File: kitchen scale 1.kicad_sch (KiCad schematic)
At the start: 1 part

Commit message: 2
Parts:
- added BT1: Battery, symbol Device:Battery
- added F1: Fuse, symbol Device:Fuse
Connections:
- new net: BT1.1 (+), F1.2
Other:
- note added: "Power"
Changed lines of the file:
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@@
 	(generator_version "9.0")
 	(paper "A4")
+	(text "Power"
+		(exclude_from_sim no)
+		(at 33.782 155.448 0)
+		(effects
+			(font
+				(size 1.27 1.27)
+			)
+		)
+	)
 	(wire
 		(pts
@@
 		)
 	)
+	(symbol
+		(lib_id "Device:Battery")
+		(at 27.94 173.99 0)
+		(unit 1)
+		(exclude_from_sim no)
+		(in_bom yes)
+		(on_board yes)
+		(dnp no)
+		(fields_autoplaced yes)
+		(property "Reference" "BT1"
+			(at 31.75 172.1484 0)
+			(effects
+				(font
+					(size 1.27 1.27)
+				)
+				(justify left)
+			)
+		)
+		(property "Value" "Battery"
+			(at 31.75 174.6884 0)
+			(effects
+				(font
+					(size 1.27 1.27)
+				)
+				(justify left)
+			)
+		)
+		(property "Footprint" ""
+			(at 27.94 172.466 90)
+			(effects
+				(font
+					(size 1.27 1.27)
+				)
+				(hide yes)
+			)
+		)
+		(property "Datasheet" "~"
+			(at 27.94 172.466 90)
+			(effects
+				(font
+					(size 1.27 1.27)
+				)
+				(hide yes)
+			)
+		)
+		(property "Description" "Multiple-cell battery"
+			(at 27.94 173.99 0)
+			(effects
+				(font
+					(size 1.27 1.27)
+				)
+				(hide yes)
+			)
+		)
+		(property "Sim.Device" "V"
+			(at 27.94 173.99 0)
+			(effects
+				(font
+					(size 1.27 1.27)
+				)
+				(hide yes)
+			)
+		)
+		(property "Sim.Type" "DC"
+			(at 27.94 173.99 0)
+			(effects
+				(font
+					(size 1.27 1.27)
+				)
+				(hide yes)
+			)
+		)
+		(property "Sim.Pins" "1=+ 2=-"
+			(at 27.94 173.99 0)
+			(effects
+				(font
+					(size 1.27 1.27)
+				)
+				(hide yes)
+			)
+		)
+		(pin "1"
+		)
+		(pin "2"
+		)
+		(instances
+			(project ""
+				(path "/e0ae7b4d-acc0-43ca-84de-8c29a2234f1c"
+					(reference "BT1")
+					(unit 1)
+				)
+			)
+		)
+	)
+	(symbol
+		(lib_id "Device:Fuse")
+		(at 27.94 165.1 0)
+		(unit 1)
+		(exclude_from_sim no)
+		(in_bom yes)
+		(on_board yes)
+		(dnp no)
+		(fields_autoplaced yes)
+		(property "Reference" "F1"
+			(at 30.48 163.8299 0)
+			(effects
+				(font
+					(size 1.27 1.27)
+				)
+				(justify left)
+			)
+		)
+		(property "Value" "Fuse"
+			(at 30.48 166.3699 0)
+			(effects
+				(font
+					(size 1.27 1.27)
+				)
+				(justify left)
+			)
+		)
+		(property "Footprint" ""
+			(at 26.162 165.1 90)
+			(effects
+				(font
+					(size 1.27 1.27)
+				)
+				(hide yes)
+			)
+		)
+		(property "Datasheet" "~"
+			(at 27.94 165.1 0)
+			(effects
+				(font
+					(size 1.27 1.27)
+				)
+				(hide yes)
+			)
+		)
+		(property "Description" "Fuse"
+			(at 27.94 165.1 0)
+			(effects
+				(font
+					(size 1.27 1.27)
+				)
+				(hide yes)
+			)
+		)
+		(pin "2"
+		)
+		(pin "1"
+		)
+		(instances
+			(project ""
+				(path "/e0ae7b4d-acc0-43ca-84de-8c29a2234f1c"
+					(reference "F1")
+					(unit 1)
+				)
+			)
+		)
+	)

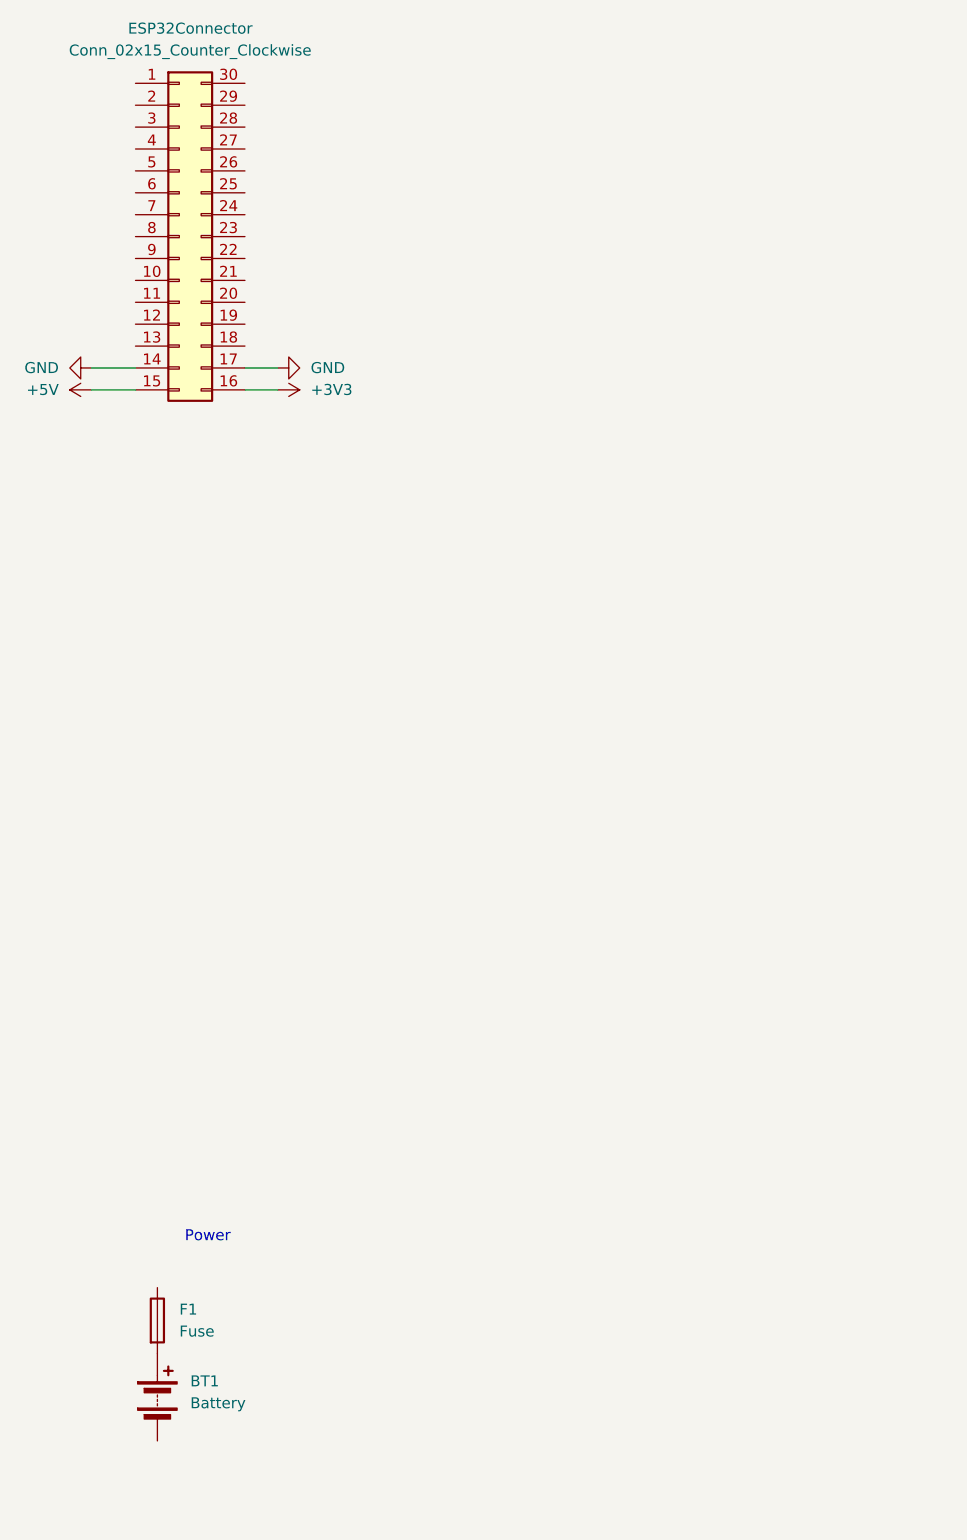
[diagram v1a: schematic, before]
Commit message: Lots of work and realized the power board should be its own thing
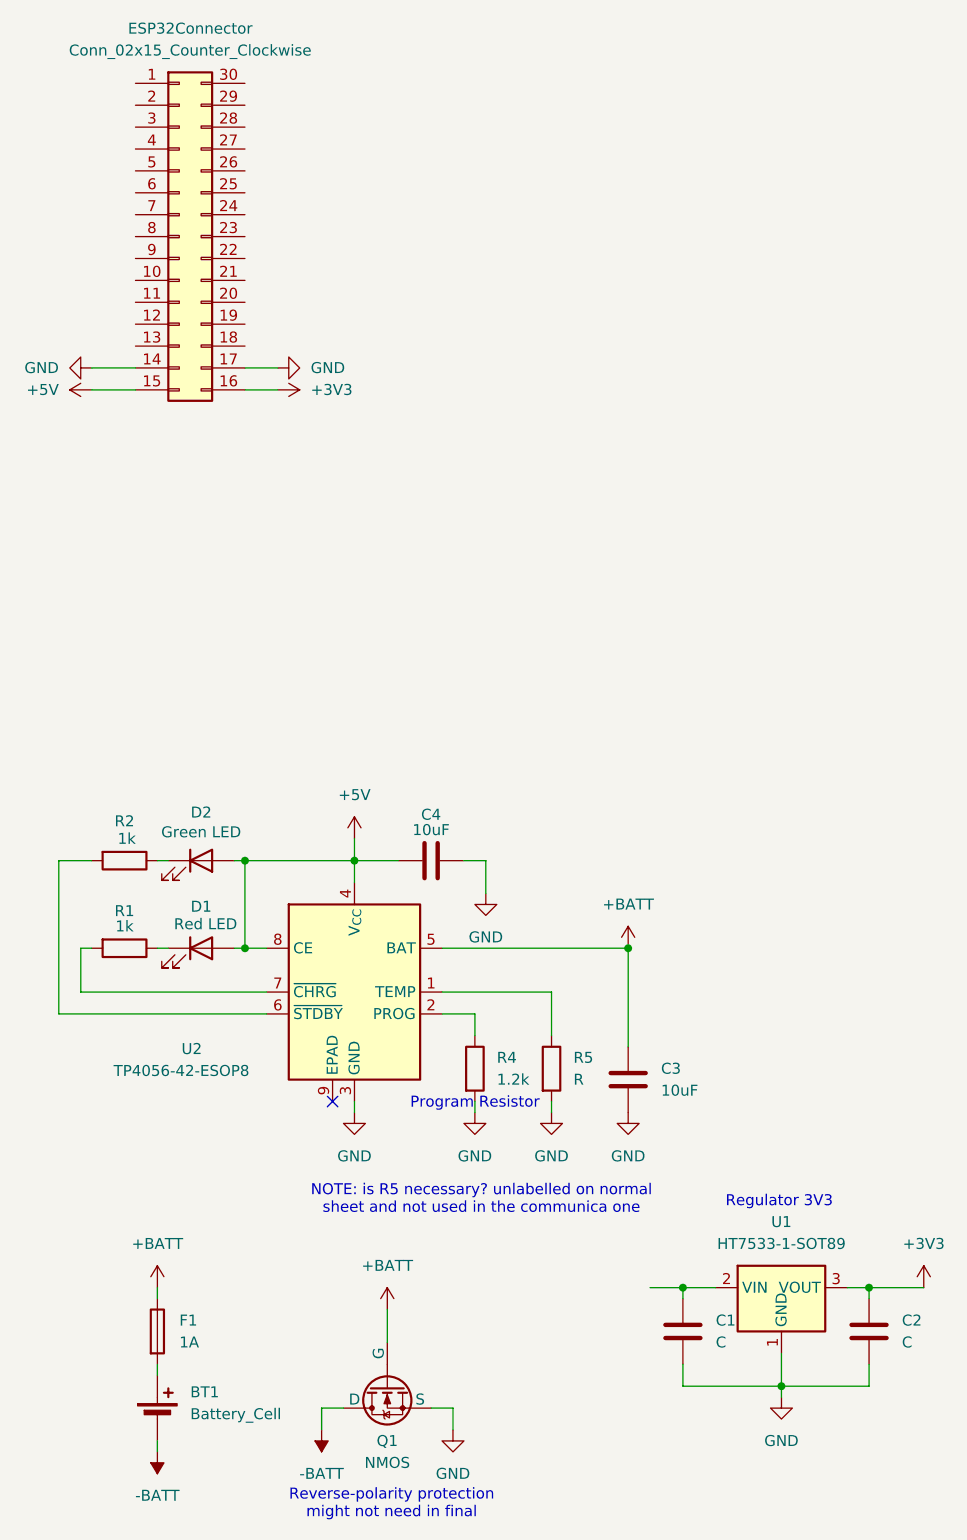
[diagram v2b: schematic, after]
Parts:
- removed BT1: Battery, symbol Device:Battery
- added BT1: Battery_Cell, symbol Device:Battery_Cell
- added C1, C2: C, symbol Device:C
- added C3, C4: 10uF, symbol Device:C
- added D1: Red LED, symbol Device:LED
- added D2: Green LED, symbol Device:LED
- added Q1: NMOS, symbol Simulation_SPICE:NMOS
- added R1, R2: 1k, symbol Device:R
- added R4: 1.2k, symbol Device:R
- added R5: R, symbol Device:R
- added U1: HT7533-1-SOT89, Package_TO_SOT_SMD:SOT-89-3, symbol Regulator_Linear:HT75xx-1-SOT89
- added U2: TP4056-42-ESOP8, Package_SO:SOIC-8-1EP_3.9x4.9mm_P1.27mm_EP2.41x3.3mm_ThermalVias, symbol Battery_Management:TP4056-42-ESOP8
- F1: value Fuse -> 1A
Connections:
- net +3V3: now also C2.1, U1.3 (VOUT)
- net +5V: now also C4.2, D1.2 (A), D2.2 (A), U2.4 (V_{CC}), U2.8 (CE)
- net GND: now also C1.2, C2.2, C3.2, C4.1, Q1.3 (S), R4.2, R5.2, U1.1 (GND), U2.3 (GND)
- net at F1.2: now also BT1.1 (+)
- net +BATT: now reaches F1.1
- net +BATT: now also C3.1, Q1.2 (G), U2.5 (BAT)
- new net: C1.1, U1.2 (VIN)
- new net: D2.1 (K), R2.1
- new net: R2.2, U2.6 (~{STDBY})
- new net: D1.1 (K), R1.1
- new net: R5.1, U2.1 (TEMP)
- new net: R4.1, U2.2 (PROG)
- new net: R1.2, U2.7 (~{CHRG})
- new net -BATT: BT1.2 (-), Q1.1 (D)
- no-connect marks 0 -> 1
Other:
- note added: "NOTE: is R5 necessary? unlabelled on normal sheet and not used in the communica one"
- note added: "Program Resistor"
- note added: "Regulator 3V3"
- note added: "Reverse-polarity protection might not need in final"
- note removed: "Power"
- moved on the sheet: F1
